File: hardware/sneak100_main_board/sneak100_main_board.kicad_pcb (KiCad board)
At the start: 2 copper layers, 68 x 75 mm, 79 parts, among them J1 Conn_01x06, J10 Conn_01x06, J11 Conn_02x03_Odd_Even, J12 Conn_02x03_Odd_Even, J13 Conn_02x05_Odd_Even, J2 Conn_01x06, J3 Conn_01x06, J4 Conn_01x06, J5 Conn_01x02, J6 Conn_01x03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

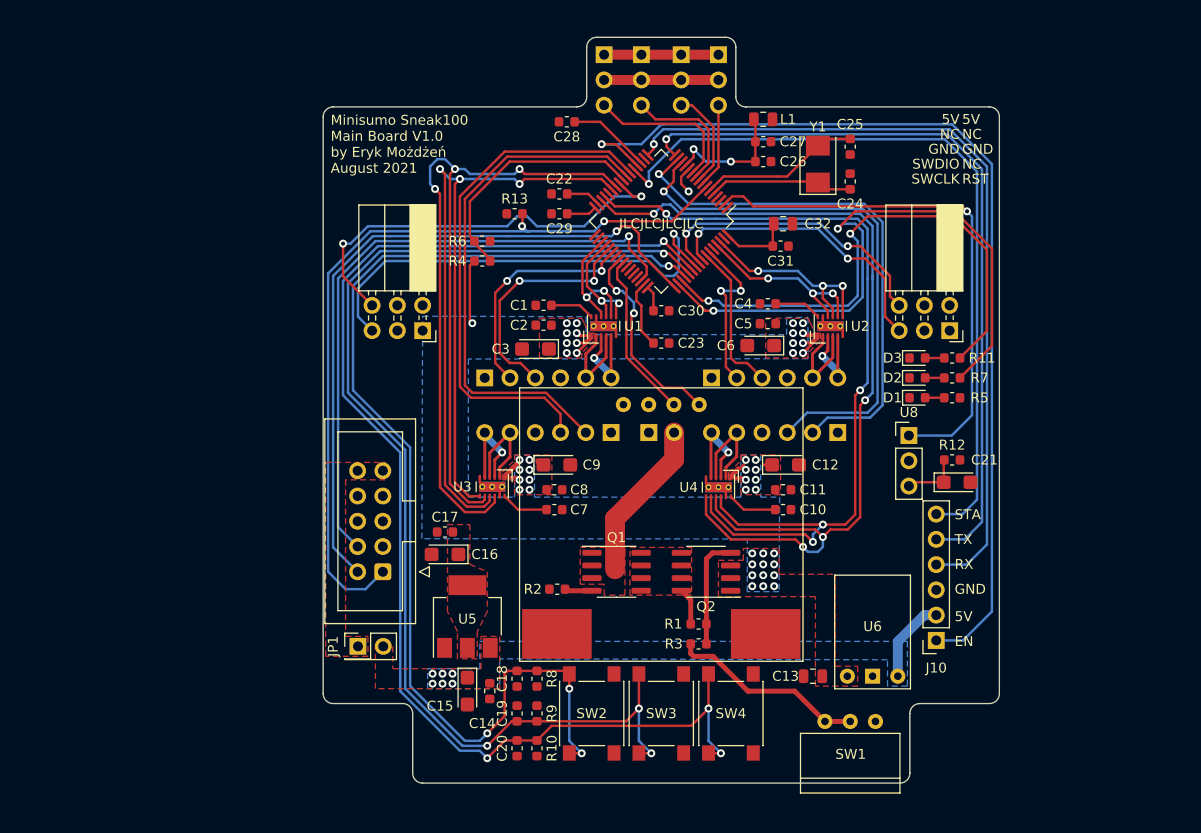
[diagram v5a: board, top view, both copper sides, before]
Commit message: ground fill zones and vias
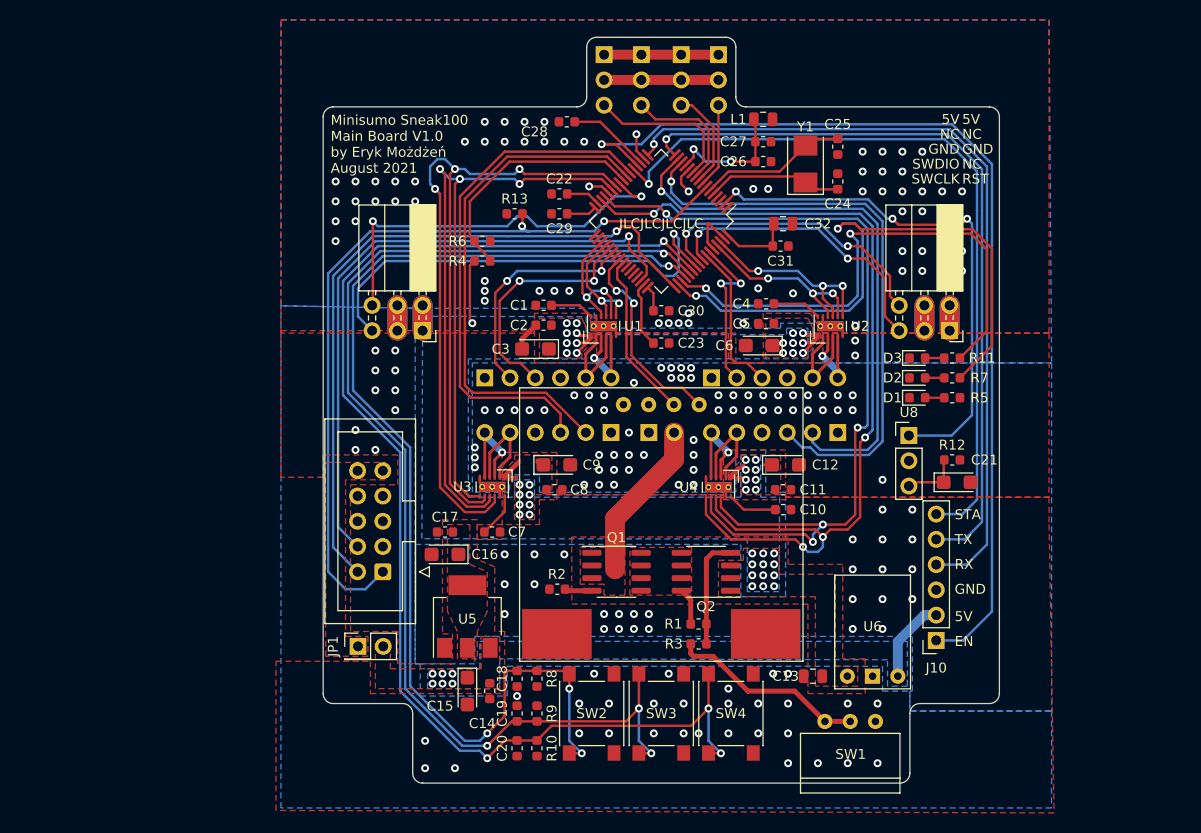
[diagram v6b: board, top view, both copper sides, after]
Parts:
- moved C7 6.64 mm to (130.8, 91.2)
- moved C24 1.25 mm to (165.5, 56.0)
- moved C25 1.25 mm to (165.5, 52.5)
- moved Y1 1.25 mm to (162.2, 54.2)
- moved C4 0.18 mm to (158.3, 68.3)
- moved C5 0.18 mm to (158.3, 70.3)
- moved C6 0.15 mm to (157.6, 72.5)
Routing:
- net GND: track 26.1 -> 49.9 mm, vias 1 -> 195
- net +3V3: track 51.8 -> 61.8 mm
- net /controller/RB_A: track 54.9 -> 59.2 mm
- net /controller/RB_B: track 53.7 -> 57.1 mm
- net /controller/PROXIMITY_FL: track 43.0 -> 40.5 mm
- net /interface/LED_ERROR: track 53.6 -> 52.2 mm
- net Net-(C25-Pad1): track 16.2 -> 15.0 mm
- net /interface/LED_RUN: track 62.0 -> 60.9 mm
- net Net-(C24-Pad1): track 14.6 -> 13.9 mm
- net /controller/RECEIVER_OUT: track 53.3 -> 53.9 mm, vias 1 -> 3
- added copper zone on B.Cu, net GND
- added copper zone on F.Cu, net GND

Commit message: 3.3V power lines
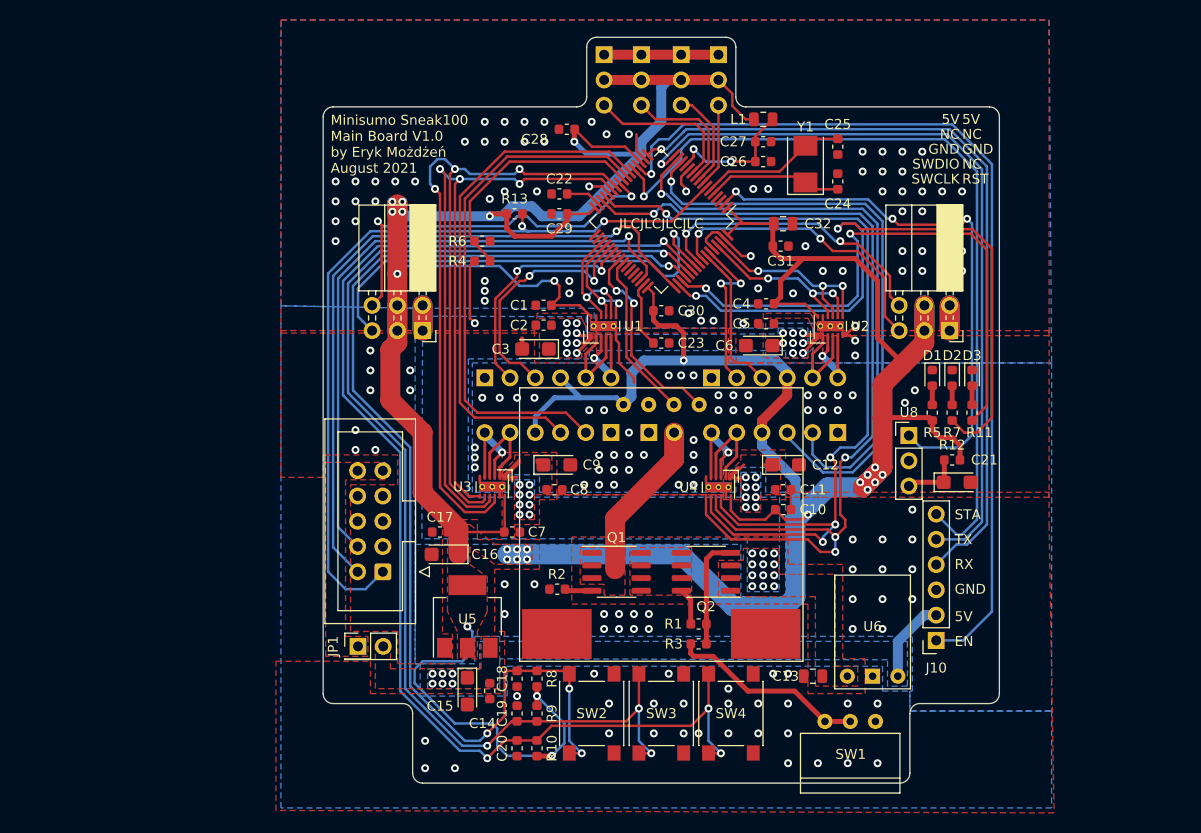
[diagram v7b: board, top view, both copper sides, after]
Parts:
- moved D3 5.85 mm to (179.0, 75.8), turned to 270 degrees
- moved R11 5.85 mm to (179.0, 79.2), turned to 270 degrees
- moved D2 3.50 mm to (177.0, 75.8), turned to 270 degrees
- moved R7 3.50 mm to (177.0, 79.2), turned to 270 degrees
- moved D1 2.50 mm to (175.0, 75.8), turned to 270 degrees
- moved R5 2.50 mm to (175.0, 79.2), turned to 90 degrees
- moved C7 2.00 mm to (132.8, 91.2)
- moved C28 0.75 mm to (138.2, 50.8)
- moved C17 0.50 mm to (125.5, 91.2)
- turned L1 to 0 degrees
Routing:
- net +3V3: track 61.8 -> 404.5 mm, vias 0 -> 25
- net GND: track 49.9 -> 61.2 mm, vias 195 -> 173
- net /interface/LED_RUN: track 60.9 -> 68.7 mm
- net /interface/LED_ERROR: track 52.2 -> 57.9 mm
- net /controller/BLUETOOTH_EN: track 98.0 -> 93.2 mm
- net /controller/BLUETOOTH_STATUS: track 76.8 -> 81.6 mm
- net /controller/RECEIVER_OUT: track 53.9 -> 56.0 mm
- net /controller/RB_B: track 57.1 -> 59.2 mm
- net /controller/RB_IN2: track 92.9 -> 94.9 mm
- net /interface/BLUETOOTH_TX: track 81.3 -> 79.5 mm
- net /controller/PROXIMITY_FL: track 40.5 -> 38.7 mm
- net /controller/RB_A: track 59.2 -> 61.0 mm
- net /interface/BLUETOOTH_RX: track 76.2 -> 77.6 mm
- net /controller/RB_IN1: track 88.3 -> 89.7 mm
- net /controller/LB_B: track 51.7 -> 52.6 mm
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
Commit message: Silk layer text
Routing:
- net +3V3: track 404.5 -> 403.8 mm
- net /controller/LF_A: track 24.9 -> 24.3 mm
- net GND: vias 173 -> 177
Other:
- board text added: "3.3V"
- board text added: "A"
- board text added: "B"
- board text added: "M1"
- board text added: "M2"
- board text added: "OUT"
- board text added: "S"
- board text added: "SUPPLY"
- board text added: "VIN"
- board text added: "VS"
